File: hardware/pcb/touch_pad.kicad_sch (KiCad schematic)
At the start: 0 parts

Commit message: small changes
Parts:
- added U7: DRV2605LDGS, Package_SO:TSSOP-10_3x3mm_P0.5mm, symbol Driver:DRV2605LDGS
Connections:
- new net: U7.10 (VDD), U7.6 (VDD/NC)
- new net GND: U7.8 (GND)
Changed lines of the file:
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@@
 	(generator_version "10.0")
 	(paper "A4")
+	(wire
+		(pts
+			(xy 130.81 87.63) (xy 130.81 88.9)
+		)
+		(stroke
+			(width 0)
+			(type default)
+		)
+	)
+	(wire
+		(pts
+			(xy 130.81 109.22) (xy 130.81 110.49)
+		)
+		(stroke
+			(width 0)
+			(type default)
+		)
+	)
+	(wire
+		(pts
+			(xy 128.27 88.9) (xy 128.27 87.63)
+		)
+		(stroke
+			(width 0)
+			(type default)
+		)
+	)
+	(wire
+		(pts
+			(xy 128.27 87.63) (xy 130.81 87.63)
+		)
+		(stroke
+			(width 0)
+			(type default)
+		)
+	)
+	(symbol
+		(lib_id "power:GND")
+		(at 130.81 110.49 0)
+		(unit 1)
+		(body_style 1)
+		(exclude_from_sim no)
+		(in_bom yes)
+		(on_board yes)
+		(in_pos_files yes)
+		(dnp no)
+		(property "Reference" "#PWR097"
+			(at 130.81 116.84 0)
+			(hide yes)
+			(show_name no)
+			(do_not_autoplace no)
+			(effects
+				(font
+					(size 1.27 1.27)
+				)
+			)
+		)
+		(property "Value" "GND"
+			(at 127.508 112.522 0)
+			(show_name no)
+			(do_not_autoplace no)
+			(effects
+				(font
+					(size 1.27 1.27)
+				)
+			)
+		)
+		(property "Footprint" ""
+			(at 130.81 110.49 0)
+			(hide yes)
+			(show_name no)
+			(do_not_autoplace no)
+			(effects
+				(font
+					(size 1.27 1.27)
+				)
+			)
+		)
+		(property "Datasheet" ""
+			(at 130.81 110.49 0)
+			(hide yes)
+			(show_name no)
+			(do_not_autoplace no)
+			(effects
+				(font
+					(size 1.27 1.27)
+				)
+			)
+		)
+		(property "Description" "Power symbol creates a global label with name \"GND\" , ground"
+			(at 130.81 110.49 0)
+			(hide yes)
+			(show_name no)
+			(do_not_autoplace no)
+			(effects
+				(font
+					(size 1.27 1.27)
+				)
+			)
+		)
+		(pin "1"
+		)
+		(instances
+			(project "meko"
+				(path "/da54f10a-146b-4941-a9c7-55c7173bb101/7a0a8608-fb91-40ee-9ae1-ac8166908c37"
+					(reference "#PWR097")
+					(unit 1)
+				)
+			)
+		)
+	)
+	(symbol
+		(lib_id "Driver:DRV2605LDGS")
+		(at 130.81 99.06 0)
+		(unit 1)
+		(body_style 1)
+		(exclude_from_sim no)
+		(in_bom yes)
+		(on_board yes)
+		(in_pos_files yes)
+		(dnp no)
+		(fields_autoplaced yes)
+		(property "Reference" "U7"
+			(at 132.9533 109.22 0)
+			(show_name no)
+			(do_not_autoplace no)
+			(effects
+				(font
+					(size 1.27 1.27)
+				)
+				(justify left)
+			)
+		)
+		(property "Value" "DRV2605LDGS"
+			(at 132.9533 111.76 0)
+			(show_name no)
+			(do_not_autoplace no)
+			(effects
+				(font
+					(size 1.27 1.27)
+				)
+				(justify left)
+			)
+		)
+		(property "Footprint" "Package_SO:TSSOP-10_3x3mm_P0.5mm"
+			(at 130.81 99.06 0)
+			(hide yes)
+			(show_name no)
+			(do_not_autoplace no)
+			(effects
+				(font
+					(size 1.27 1.27)
+					(italic yes)
+				)
+			)
+		)
+		(property "Datasheet" "http://www.ti.com/lit/ds/symlink/drv2605l.pdf"
+			(at 130.81 99.06 0)
+			(hide yes)
+			(show_name no)
+			(do_not_autoplace no)
+			(effects
+				(font
+					(size 1.27 1.27)
+				)
+			)
+		)
+		(property "Description" "Haptic driver for LRAs and ERMs with effect library, 2-5.2V, TSSOP-10 (Texas DGS0010A / VSSOP)"
+			(at 130.81 99.06 0)
+			(hide yes)
+			(show_name no)
+			(do_not_autoplace no)
+			(effects
+				(font
+					(size 1.27 1.27)
+				)
+			)
+		)
+		(pin "3"
+		)
+		(pin "10"
+		)
+		(pin "9"
+		)
+		(pin "8"
+		)
+		(pin "7"
+		)
+		(pin "1"
+		)
+		(pin "5"
+		)
+		(pin "6"
+		)
+		(pin "2"
+		)
+		(pin "4"
+		)
+		(instances
+			(project "meko"
+				(path "/da54f10a-146b-4941-a9c7-55c7173bb101/7a0a8608-fb91-40ee-9ae1-ac8166908c37"
+					(reference "U7")
+					(unit 1)
+				)
+			)
+		)
+	)
 )

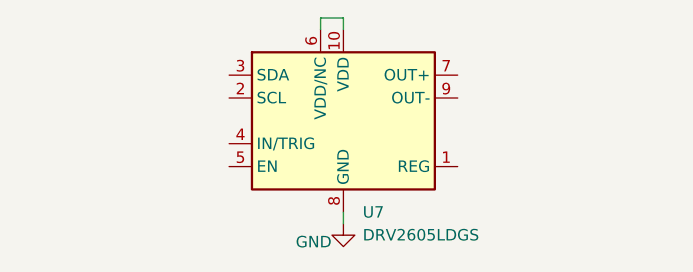
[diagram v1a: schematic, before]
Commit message: assigning pins
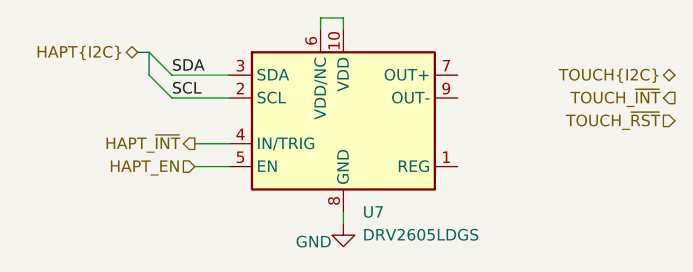
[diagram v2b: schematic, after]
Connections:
- net SCL: now reaches U7.2 (SCL)
- net SDA: now reaches U7.3 (SDA)
- net HAPT_~{INT}: now reaches U7.4 (IN/TRIG)
- net HAPT_EN: now reaches U7.5 (EN)
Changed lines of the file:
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@@
 	(generator_version "10.0")
 	(paper "A4")
+	(bus_entry
+		(at 109.22 93.98)
+		(size 2.54 2.54)
+		(stroke
+			(width 0)
+			(type default)
+		)
+	)
+	(bus_entry
+		(at 109.22 91.44)
+		(size 2.54 2.54)
+		(stroke
+			(width 0)
+			(type default)
+		)
+	)
+	(wire
+		(pts
+			(xy 111.76 93.98) (xy 118.11 93.98)
+		)
+		(stroke
+			(width 0)
+			(type default)
+		)
+	)
 	(wire
 		(pts
@@
 		)
 	)
+	(bus
+		(pts
+			(xy 107.95 91.44) (xy 109.22 91.44)
+		)
+		(stroke
+			(width 0)
+			(type default)
+		)
+	)
+	(wire
+		(pts
+			(xy 114.3 101.6) (xy 118.11 101.6)
+		)
+		(stroke
+			(width 0)
+			(type default)
+		)
+	)
+	(bus
+		(pts
+			(xy 109.22 91.44) (xy 109.22 93.98)
+		)
+		(stroke
+			(width 0)
+			(type default)
+		)
+	)
 	(wire
 		(pts
 			(xy 130.81 109.22) (xy 130.81 110.49)
+		)
+		(stroke
+			(width 0)
+			(type default)
+		)
+	)
+	(wire
+		(pts
+			(xy 114.3 104.14) (xy 118.11 104.14)
+		)
+		(stroke
+			(width 0)
+			(type default)
+		)
+	)
+	(wire
+		(pts
+			(xy 111.76 96.52) (xy 118.11 96.52)
 		)
 		(stroke
@@
 		)
 	)
+	(label "SDA"
+		(at 111.76 93.98 0)
+		(effects
+			(font
+				(size 1.27 1.27)
+			)
+			(justify left bottom)
+		)
+	)
+	(label "SCL"
+		(at 111.76 96.52 0)
+		(effects
+			(font
+				(size 1.27 1.27)
+			)
+			(justify left bottom)
+		)
+	)
+	(hierarchical_label "TOUCH_~{RST}"
+		(shape input)
+		(at 167.64 99.06 180)
+		(effects
+			(font
+				(size 1.27 1.27)
+			)
+			(justify right)
+		)
+	)
+	(hierarchical_label "HAPT{I2C}"
+		(shape bidirectional)
+		(at 107.95 91.44 180)
+		(effects
+			(font
+				(size 1.27 1.27)
+			)
+			(justify right)
+		)
+	)
+	(hierarchical_label "TOUCH_~{INT}"
+		(shape output)
+		(at 167.64 96.52 180)
+		(effects
+			(font
+				(size 1.27 1.27)
+			)
+			(justify right)
+		)
+	)
+	(hierarchical_label "HAPT_~{INT}"
+		(shape output)
+		(at 114.3 101.6 180)
+		(effects
+			(font
+				(size 1.27 1.27)
+			)
+			(justify right)
+		)
+	)
+	(hierarchical_label "HAPT_EN"
+		(shape input)
+		(at 114.3 104.14 180)
+		(effects
+			(font
+				(size 1.27 1.27)
+			)
+			(justify right)
+		)
+	)
+	(hierarchical_label "TOUCH{I2C}"
+		(shape bidirectional)
+		(at 167.64 93.98 180)
+		(effects
+			(font
+				(size 1.27 1.27)
+			)
+			(justify right)
+		)
+	)

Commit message: main board: removed touch_rst label
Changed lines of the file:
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@@
-		)
-	)
-	(hierarchical_label "TOUCH_~{RST}"
-		(shape input)
-		(at 167.64 99.06 180)
-		(effects
-			(font
-				(size 1.27 1.27)
-			)
-			(justify right)
 		)
 	)
@@
 	)
 	(hierarchical_label "TOUCH_~{INT}"
-		(shape output)
+		(shape bidirectional)
 		(at 167.64 96.52 180)
 		(effects
